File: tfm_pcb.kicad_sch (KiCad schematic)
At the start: 70 parts, among them J1 Conn_01x02_MountingPin, J12 Conn_01x01_Pin, J13 Conn_01x01_Pin, J15 Conn_01x01_Socket, J16 Conn_01x01_Socket, J17 Conn_01x01_Socket, J18 Conn_01x01_Socket, J19 Conn_01x01_Socket, J2 USB_B_Micro, J20 Conn_01x01_Socket, J21 Conn_01x01_Socket, J22 Conn_01x01_Socket, J23 Conn_01x01_Socket, J24 Conn_01x01_Socket, J3 Mounting Pin, J5 Conn_01x01_Pin, J6 Conn_01x01_Pin, U1 ESP32-S3-WROOM-2, U2 MCP73871-2CC, U3 ADS1292IPBS, U4 LSM6DS3, U5 USBLC6-2SC6, U6 XC6220B331MR, U7 USBLC6-2SC6

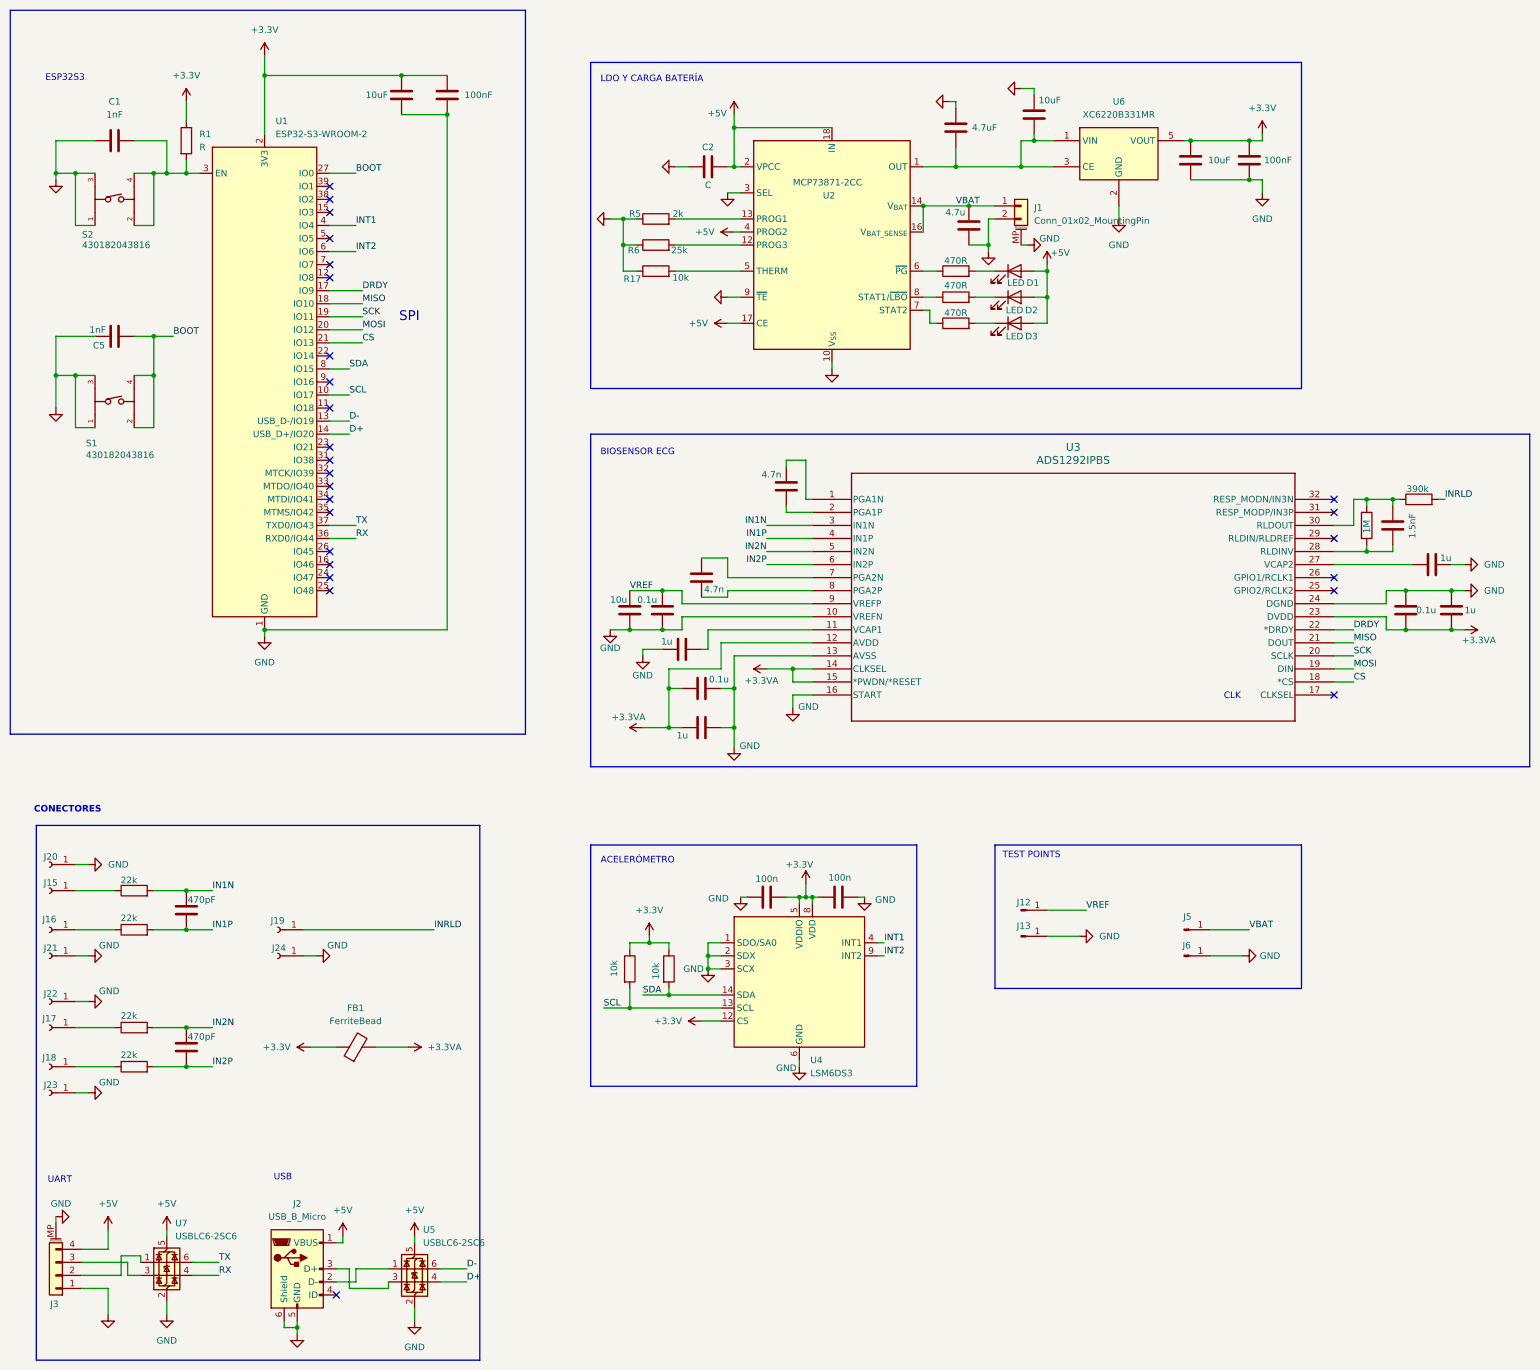
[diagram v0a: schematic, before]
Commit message: Separar DVDD de la ferrita, filtro amortiguado en AVDD y conector THT de electrodos
- DVDD del ADS1292 (y C6/C7) a +3.3V sin ferrita.
- Rama analógica: FB1 + R15 (2.2 ohm) + C26 (10 uF) antes de AVDD; filtro
  colocado junto al AFE manteniendo el puente en B.Cu bajo el ADS1292.
- C12 (VREFP) sincronizado a 10 uF en la PCB.
- Esquemático: pastillas de electrodos sustituidas por conector THT 1x10.
- Documentación movida a docs_local/ (ignorada por git).

Co-Authored-By: Claude Opus 5.5 <noreply@anthropic.com>
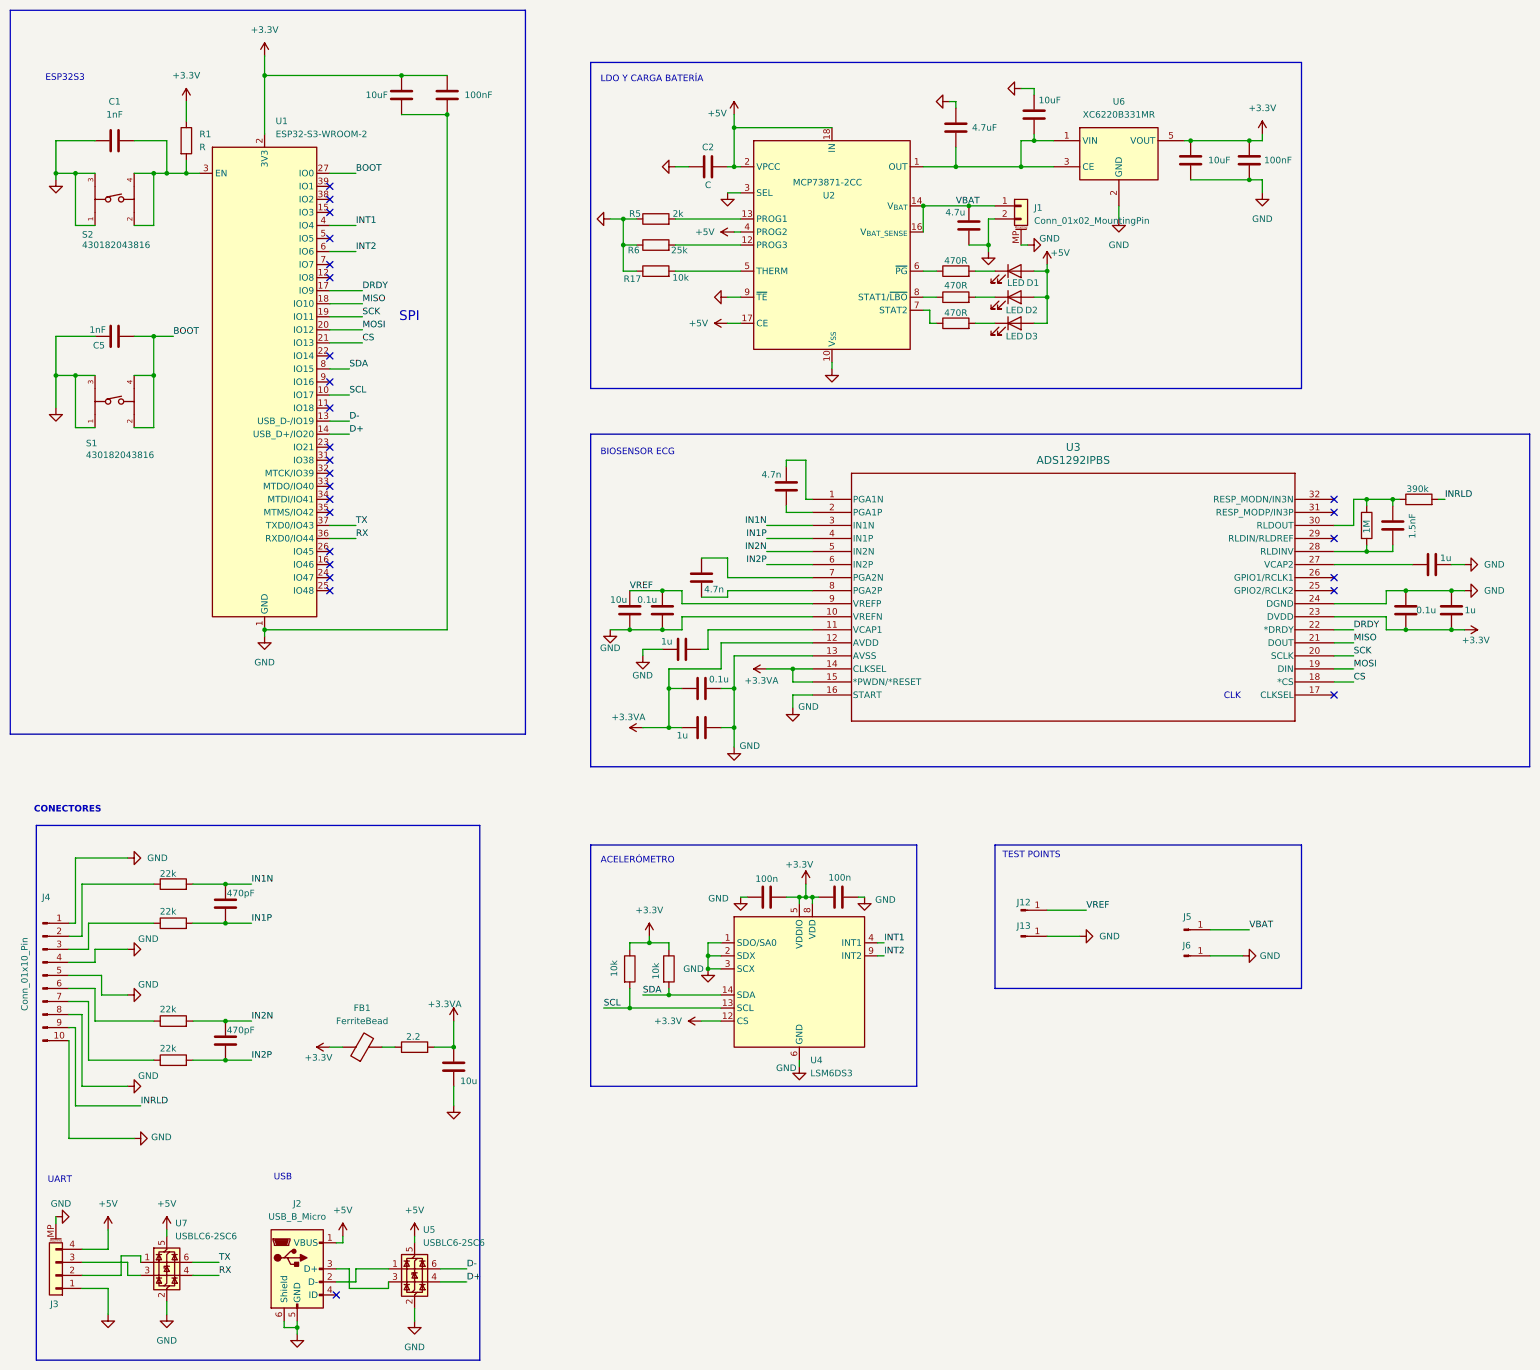
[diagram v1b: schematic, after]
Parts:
- removed J15, J16, J17, J18, J19, J20, J21, J22, J23, J24: Conn_01x01_Socket, Connector_Wire:SolderWirePad_1x01_SMD_2x4mm, symbol Connector:Conn_01x01_Socket
- added C26: 10u, Capacitor_SMD:C_0805_2012Metric, symbol Device:C
- added J4: Conn_01x10_Pin, Connector_PinHeader_2.54mm:PinHeader_1x10_P2.54mm_Vertical, symbol Connector:Conn_01x10_Pin
- added R15: 2.2, Resistor_SMD:R_0603_1608Metric, symbol Device:R
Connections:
- net +3.3V: now also C6.2, C7.2, U3.23 (DVDD)
- net +3.3VA: now also C26.1, R15.2; no longer C6.2, C7.2, FB1.2, U3.23 (DVDD)
- net GND: now also C26.2, J4.1 (Pin_1), J4.10 (Pin_10), J4.4 (Pin_4), J4.5 (Pin_5), J4.8 (Pin_8)
- net INRLD: now also J4.9 (Pin_9)
- net at R8.1: now also J4.3 (Pin_3)
- net at R9.1: now also J4.6 (Pin_6)
- net at R10.1: now also J4.7 (Pin_7)
- net at R7.1: now also J4.2 (Pin_2)
- new net: FB1.2, R15.1
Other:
- moved on the sheet: FB1

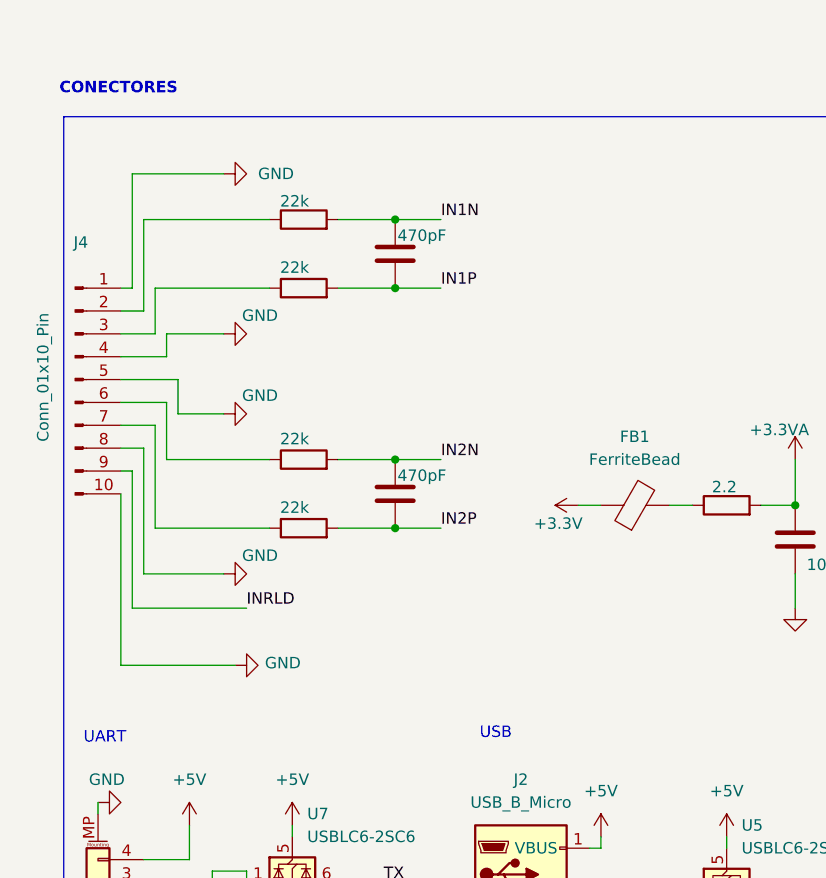
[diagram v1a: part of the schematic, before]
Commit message: Conector J4 THT reordenado, selector de malla JP1 y net SHIELD
- J4 (tira 1x10): 1 RLD, 2-3 malla, 4 IN1N, 5 IN1P, 6-7 malla, 8 IN2N,
  9 IN2P, 10 malla; etiquetas EL1N/EL1P/EL2N/EL2P en lugar del abanico.
- Net SHIELD con las cinco mallas; JP1 (tira 3 pines): 1-2 INRLD (T2),
  2-3 GND (T1). Serigrafía de función en J4 y JP1.
- Ajustes de layout del autor: filtro FB1/R15/C26 junto a C9, C26 en
  0603, SHIELD por B.Cu en el borde, rutado de EL2P.

Co-Authored-By: Claude Opus 5.5 <noreply@anthropic.com>
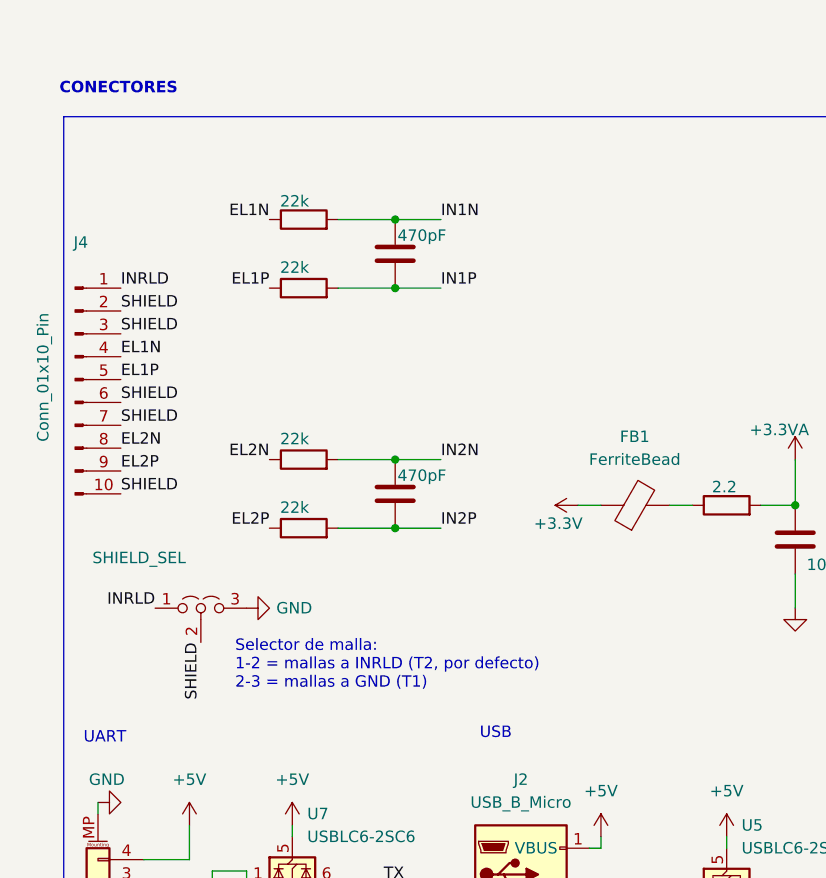
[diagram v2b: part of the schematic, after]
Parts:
- added JP1: SHIELD_SEL, Connector_PinHeader_2.54mm:PinHeader_1x03_P2.54mm_Vertical, symbol Jumper:Jumper_3_Open
- C26: footprint Capacitor_SMD:C_0805_2012Metric -> Capacitor_SMD:C_0603_1608Metric
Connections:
- net GND: now also JP1.3 (B); no longer J4.1 (Pin_1), J4.10 (Pin_10), J4.4 (Pin_4), J4.5 (Pin_5), J4.8 (Pin_8)
- net INRLD: now also J4.1 (Pin_1), JP1.1 (A); no longer J4.9 (Pin_9)
- net EL1P: now reaches R8.1
- net EL1P: now also J4.5 (Pin_5); no longer J4.3 (Pin_3)
- net EL2P: now reaches R10.1
- net EL2P: now also J4.9 (Pin_9); no longer J4.7 (Pin_7)
- net EL1N: now reaches R7.1
- net EL1N: now also J4.4 (Pin_4); no longer J4.2 (Pin_2)
- net EL2N: now reaches R9.1
- net EL2N: now also J4.8 (Pin_8); no longer J4.6 (Pin_6)
- new net SHIELD: J4.10 (Pin_10), J4.2 (Pin_2), J4.3 (Pin_3), J4.6 (Pin_6), J4.7 (Pin_7), JP1.2 (C)
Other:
- note added: "Selector de malla: 1-2 = mallas a INRLD (T2, por defecto) 2-3 = mallas a GND (T1)"

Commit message: PWDN del ADS1292 controlado por IO38 y reordenado del desacoplo de AVDD
- PWDN/RESET (U3.15) separado de +3.3VA y llevado a IO38 (U1.31) con
  pull-down R16 = 10 kOhm; rutado por la derecha del bus SPI con salto
  en B.Cu bajo la pista de BOOT.
- CLKSEL (U3.14) sigue en +3.3VA.
- Ajustes de layout del autor: cadena AVDD R15 -> C26 -> C9 -> C8 -> pin,
  vías de GND junto a los condensadores, vías de cosido recolocadas y
  START (U3.16) unido al plano por el relleno de cobre.

Co-Authored-By: Claude Opus 5.5 <noreply@anthropic.com>
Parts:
- added R16: 10k, Resistor_SMD:R_0603_1608Metric, symbol Device:R
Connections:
- net +3.3VA: no longer U3.15 (*PWDN/*RESET)
- net GND: now also R16.2
- net ADS_PWDN: now reaches U1.31 (IO38)
- net ADS_PWDN: now also U3.15 (*PWDN/*RESET), R16.1
- no-connect marks 26 -> 25
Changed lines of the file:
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@@
 	)
 	(junction
-		(at 177.8 143.51)
-		(diameter 0)
-		(color 0 0 0 0)
-	)
-	(junction
 		(at 74.93 27.94)
 		(diameter 0)
@@
 	)
 	(no_connect
-		(at 87.63 102.87)
-	)
-	(no_connect
 		(at 88.9 265.43)
 	)
@@
 	(wire
 		(pts
+			(xy 170.18 146.05) (xy 181.61 146.05)
+		)
+		(stroke
+			(width 0)
+			(type default)
+		)
+	)
+	(wire
+		(pts
 			(xy 204.47 76.2) (xy 205.74 76.2)
 		)
@@
 	(wire
 		(pts
-			(xy 181.61 146.05) (xy 177.8 146.05)
-		)
-		(stroke
-			(width 0)
-			(type default)
-		)
-	)
-	(wire
-		(pts
 			(xy 293.37 135.89) (xy 297.18 135.89)
 		)
@@
 	(wire
 		(pts
+			(xy 93.98 102.87) (xy 87.63 102.87)
+		)
+		(stroke
+			(width 0)
+			(type default)
+		)
+	)
+	(wire
+		(pts
 			(xy 209.55 33.02) (xy 208.28 33.02)
 		)
@@
 	(wire
 		(pts
-			(xy 172.72 143.51) (xy 177.8 143.51)
+			(xy 172.72 143.51) (xy 181.61 143.51)
 		)
 		(stroke
@@
 	(wire
 		(pts
-			(xy 177.8 146.05) (xy 177.8 143.51)
-		)
-		(stroke
-			(width 0)
-			(type default)
-		)
-	)
-	(wire
-		(pts
 			(xy 39.37 261.62) (xy 46.99 261.62)
 		)
@@
 	(wire
 		(pts
-			(xy 177.8 143.51) (xy 181.61 143.51)
-		)
-		(stroke
-			(width 0)
-			(type default)
-		)
-	)
-	(wire
-		(pts
 			(xy 222.25 60.96) (xy 223.52 60.96)
 		)
@@
 		)
 	)
+	(label "ADS_PWDN"
+		(at 93.98 102.87 0)
+		(effects
+			(font
+				(size 1.27 1.27)
+			)
+			(justify left bottom)
+		)
+	)
 	(label "SHIELD"
 		(at 45.72 232.41 270)
@@
 		)
 	)
+	(label "ADS_PWDN"
+		(at 181.61 146.05 180)
+		(effects
+			(font
+				(size 1.27 1.27)
+			)
+			(justify right bottom)
+		)
+	)
 	(label "EL2N"
 		(at 36.83 210.82 0)
@@
 		)
 		(property "Value" "+3.3VA"
-			(at 175.006 145.796 90)
+			(at 179.07 142.24 90)
 			(show_name no)
 			(do_not_autoplace no)
@@
 	(symbol
 		(lib_id "power:GND")
+		(at 170.18 153.67 0)
+		(unit 1)
+		(body_style 1)
+		(exclude_from_sim no)
+		(in_bom yes)
+		(on_board yes)
+		(in_pos_files yes)
+		(dnp no)
+		(fields_autoplaced yes)
+		(property "Reference" "#PWR062"
+			(at 170.18 160.02 0)
+			(hide yes)
+			(show_name no)
+			(do_not_autoplace no)
+			(effects
+				(font
+					(size 1.27 1.27)
+				)
+			)
+		)
+		(property "Value" "GND"
+			(at 170.18 158.75 0)
+			(hide yes)
+			(show_name no)
+			(do_not_autoplace no)
+			(effects
+				(font
+					(size 1.27 1.27)
+				)
+			)
+		)
+		(property "Footprint" ""
+			(at 170.18 153.67 0)
+			(hide yes)
+			(show_name no)
+			(do_not_autoplace no)
+			(effects
+				(font
+					(size 1.27 1.27)
+				)
+			)
+		)
+		(property "Datasheet" ""
+			(at 170.18 153.67 0)
+			(hide yes)
+			(show_name no)
+			(do_not_autoplace no)
+			(effects
+				(font
+					(size 1.27 1.27)
+				)
+			)
+		)
+		(property "Description" "Power symbol creates a global label with name \"GND\" , ground"
+			(at 170.18 153.67 0)
+			(hide yes)
+			(show_name no)
+			(do_not_autoplace no)
+			(effects
+				(font
+					(size 1.27 1.27)
+				)
+			)
+		)
+		(pin "1"
+		)
+		(instances
+			(project "tfm_pcb"
+				(path "/4cd6c202-e313-4beb-89da-bfd55e6bd2cf"
+					(reference "#PWR062")
+					(unit 1)
+				)
+			)
+		)
+	)
+	(symbol
+		(lib_id "power:GND")
 		(at 165.1 50.8 0)
 		(unit 1)
@@
 					(unit 1)
 				)
+			)
+		)
+	)
+	(symbol
+		(lib_id "Device:R")
+		(at 170.18 149.86 0)
+		(unit 1)
+		(body_style 1)
+		(exclude_from_sim no)
+		(in_bom yes)
+		(on_board yes)
+		(in_pos_files yes)
+		(dnp no)
+		(property "Reference" "R16"
+			(at 172.72 148.59 0)
+			(hide yes)
+			(show_name no)
+			(do_not_autoplace no)
+			(effects
+				(font
+					(size 1.27 1.27)
+				)
+				(justify left)
+			)
+		)
+		(property "Value" "10k"
+			(at 167.64 151.892 90)
+			(show_name no)
+			(do_not_autoplace no)
+			(effects
+				(font
+					(size 1.27 1.27)
+				)
+				(justify left)
+			)
+		)
+		(property "Footprint" "Resistor_SMD:R_0603_1608Metric"
+			(at 168.402 149.86 90)
+			(hide yes)
+			(show_name no)
+			(do_not_autoplace no)
+			(effects
+				(font
+					(size 1.27 1.27)
+				)
+			)
+		)
+		(property "Datasheet" ""
+			(at 170.18 149.86 0)
+			(hide yes)
+			(show_name no)
+			(do_not_autoplace no)
+			(effects
+				(font
+					(size 1.27 1.27)
+				)
+			)
+		)
+		(property "Description" "Resistor"
+			(at 170.18 149.86 0)
+			(hide yes)
+			(show_name no)
+			(do_not_autoplace no)
+			(effects
+				(font
+					(size 1.27 1.27)
+				)
+			)
+		)
+		(pin "1"
+		)
+		(pin "2"
+		)
+		(instances
+			(project "tfm_pcb"
+				(path "/4cd6c202-e313-4beb-89da-bfd55e6bd2cf"
+					(reference "R16")
+					(unit 1)
+				)

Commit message: Arreglos previos a fabricación: pines sin usar del ADS1292, EN, C2, vías térmicas y masas
- ADS1292: IN3P/IN3N/RLDIN a AVDD (pista bajo el encapsulado desde el pin 12);
  GPIO1/GPIO2 a DGND con R19/R18 de 10 kOhm.
- ESP32 EN: R1 = 10 kOhm, C1 = 1 uF a 4.5 mm del pin.
- MCP73871: C2 = 10 uF en 0805; huella con 4 vías térmicas de 0.3 mm.
- U4: vías de GND para sus pads de masa; conexión sólida al plano en
  U5/U6/U7/J2/R18/R19. DRC sin errores.

Co-Authored-By: Claude Opus 5.5 <noreply@anthropic.com>
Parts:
- added R18, R19: 10k, Resistor_SMD:R_0603_1608Metric, symbol Device:R
- C1: value 1nF -> 1u
- C2: value C -> 10u; footprint Capacitor_SMD:C_0603_1608Metric -> Capacitor_SMD:C_0805_2012Metric
- R1: value R -> 10k
- U2: footprint Package_DFN_QFN:QFN-20-1EP_4x4mm_P0.5mm_EP2.5x2.5mm -> Package_DFN_QFN:QFN-20-1EP_4x4mm_P0.5mm_EP2.5x2.5mm_ThermalVias
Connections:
- net +3.3VA: now also U3.29 (RLDIN/RLDREF), U3.31 (RESP_MODP/IN3P), U3.32 (RESP_MODN/IN3N)
- net GND: now also R18.2, R19.2
- net at U3.25 (GPIO2/RCLK2): now also R18.1
- net at U3.26 (GPIO1/RCLK1): now also R19.1
- no-connect marks 25 -> 20

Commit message: Reorganización de layout del autor: zona ADS1292, SPI, acelerómetro y +3.3V
- Recolocación de la zona del ADS1292 (C8, C9, C10, C11, C18, C26, R11,
  R12, R15, R18, R19) y nuevo rutado de SPI a 0.25 mm.
- Acelerómetro U4 recolocado, con vía de GND central e INT1 por F.Cu.
- Tronco de +3.3V y alimentación del filtro de AVDD rehechos.
- C8 a 0402 en el esquemático; ancho de pista 0.25 mm añadido al proyecto.

Pendiente: C11 en 0402 en la PCB y 0603 en el esquemático (paridad),
alivio térmico del pad 7 de U4 y dos pistas colgando (+5V, +3.3V).

Co-Authored-By: Claude Opus 5.5 <noreply@anthropic.com>
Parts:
- C8: footprint Capacitor_SMD:C_0603_1608Metric -> Capacitor_SMD:C_0402_1005Metric

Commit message: Condensadores del ADS1292 en 0402 (C8, C11, C12, C13) y recolocación de VREF
- Esquemático y PCB sincronizados: C8, C11, C12 y C13 en 0402.
- C12/C13 (VREFP) más cerca del pin 9; punto de prueba de VREF recolocado.
- Retoques de rutado del autor en VREF, GND, +3.3V, +3.3VA, RX y EN.

Pendiente: el punto de prueba J12 aparece como "VREF" solo en la PCB
(paridad); alivios térmicos de C11.2 y U4.7; dos pistas colgando.

Co-Authored-By: Claude Opus 5.5 <noreply@anthropic.com>
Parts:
- C11, C12, C13: footprint Capacitor_SMD:C_0603_1608Metric -> Capacitor_SMD:C_0402_1005Metric
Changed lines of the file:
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@@
 			)
 		)
-		(property "Footprint" "Capacitor_SMD:C_0603_1608Metric"
+		(property "Footprint" "Capacitor_SMD:C_0402_1005Metric"
 			(at 145.0848 128.27 0)
 			(hide yes)
@@
 			)
 		)
-		(property "Footprint" "Capacitor_SMD:C_0603_1608Metric"
+		(property "Footprint" "Capacitor_SMD:C_0402_1005Metric"
 			(at 151.4348 128.27 0)
 			(hide yes)
@@
 			)
 		)
-		(property "Footprint" "Capacitor_SMD:C_0603_1608Metric"
+		(property "Footprint" "Capacitor_SMD:C_0402_1005Metric"
 			(at 152.4 140.6652 0)
 			(hide yes)
